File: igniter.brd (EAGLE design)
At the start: 29.2 x 63.5 mm, 9 parts, among them X1 Break, X2 IGN1, X3 IGN2

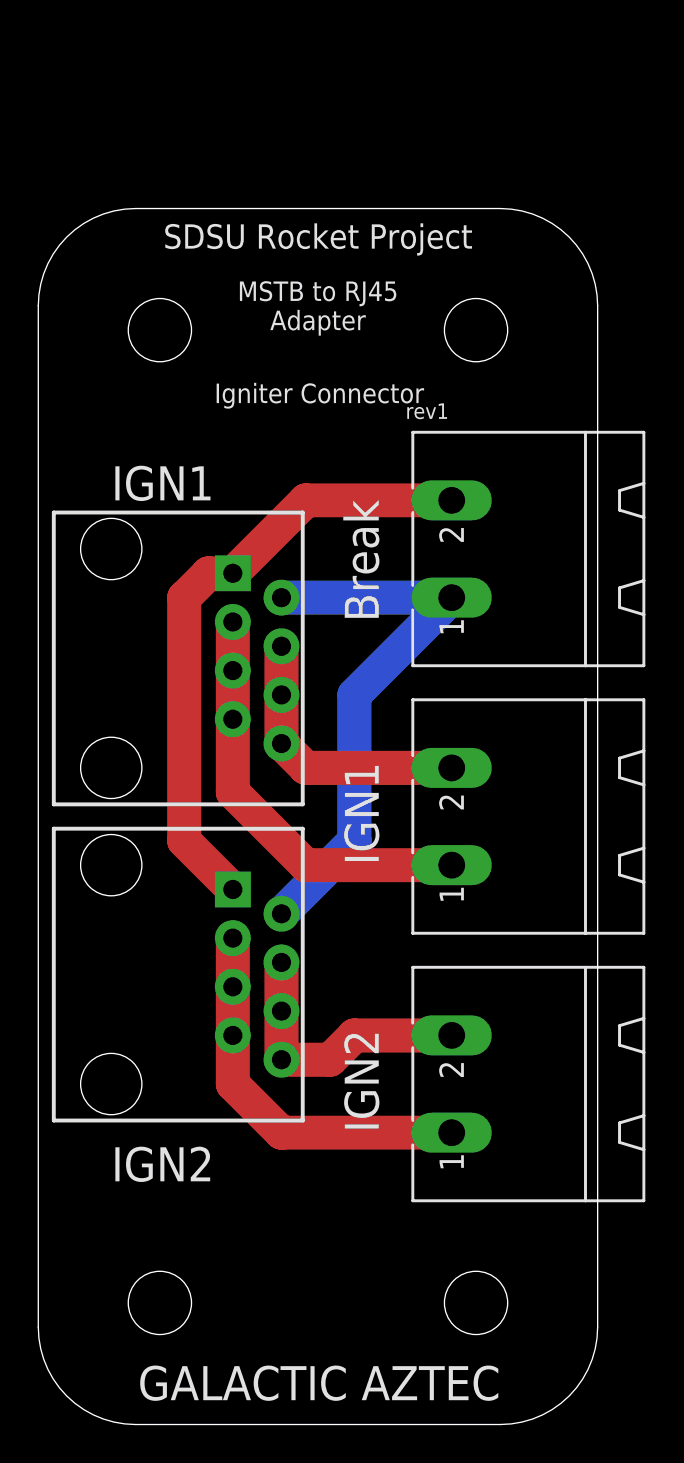
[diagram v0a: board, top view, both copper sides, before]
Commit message: Added ignition status LEDs. Separated break wire from ignition wires. Added SDSU logo.
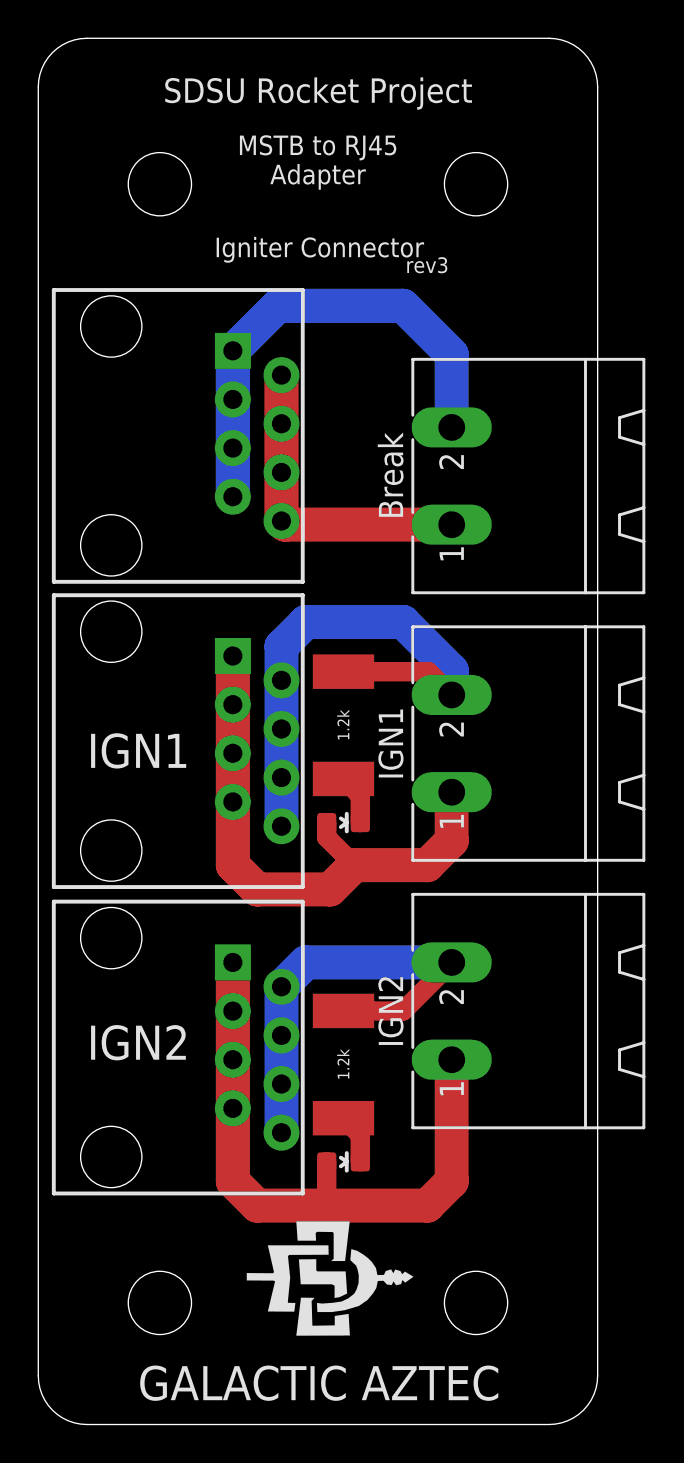
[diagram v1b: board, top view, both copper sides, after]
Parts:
- added BREAK: RJ45, SparkFun-Connectors:RJ45-8
- added D1, D2: RED, SparkFun-LED:LED-0603
- added FRAME1: (no value), SparkFun-Aesthetics:CREATIVE_COMMONS
- added R1, R2: 1.2k, SparkFun-Resistors:R2512
- moved U$3 7.62 mm to (22.9, 64.8)
- moved U$4 7.62 mm to (6.35, 64.8)
- moved IGNITER1 4.32 mm to (3.81, 35.7)
- moved IGNITER2 3.81 mm to (3.81, 19.7)
- moved X1 3.81 mm to (26.7, 49.5)
- moved X2 3.81 mm to (26.7, 35.6)
- moved X3 3.81 mm to (26.7, 21.6)
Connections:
- new net N$1: D1.C, R1.1
- new net N$2: D2.C, R2.1
- net 3V3: now also BREAK.1, BREAK.3, BREAK.5, BREAK.7; no longer IGNITER1.1, IGNITER2.1
- net BRK: now also BREAK.2, BREAK.4, BREAK.6, BREAK.8; no longer IGNITER1.2, IGNITER2.2
- net IGN1+: now also D1.A, IGNITER1.1
- net IGN1-: now also IGNITER1.2, R1.2
- net IGN2+: now also D2.A, IGNITER2.1
- net IGN2-: now also IGNITER2.2, R2.2
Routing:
- net IGN2+: track 20.1 -> 33.2 mm
- net IGN1-: track 14.5 -> 27.3 mm
- net BRK: track 29.1 -> 16.6 mm
- net IGN2-: track 14.5 -> 23.7 mm
- net 3V3: track 32.4 -> 24.9 mm
- net IGN1+: track 21.9 -> 29.3 mm
- net N$2: track 0.00 -> 2.64 mm
- net N$1: track 0.00 -> 2.64 mm
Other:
- board size 29.2 x 63.5 mm -> 29.2 x 72.4 mm
- board text added: "rev3"
- board text removed: "rev1"

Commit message: Updated to use more efficient LEDs. Decreased SMD resistor size to 0603.
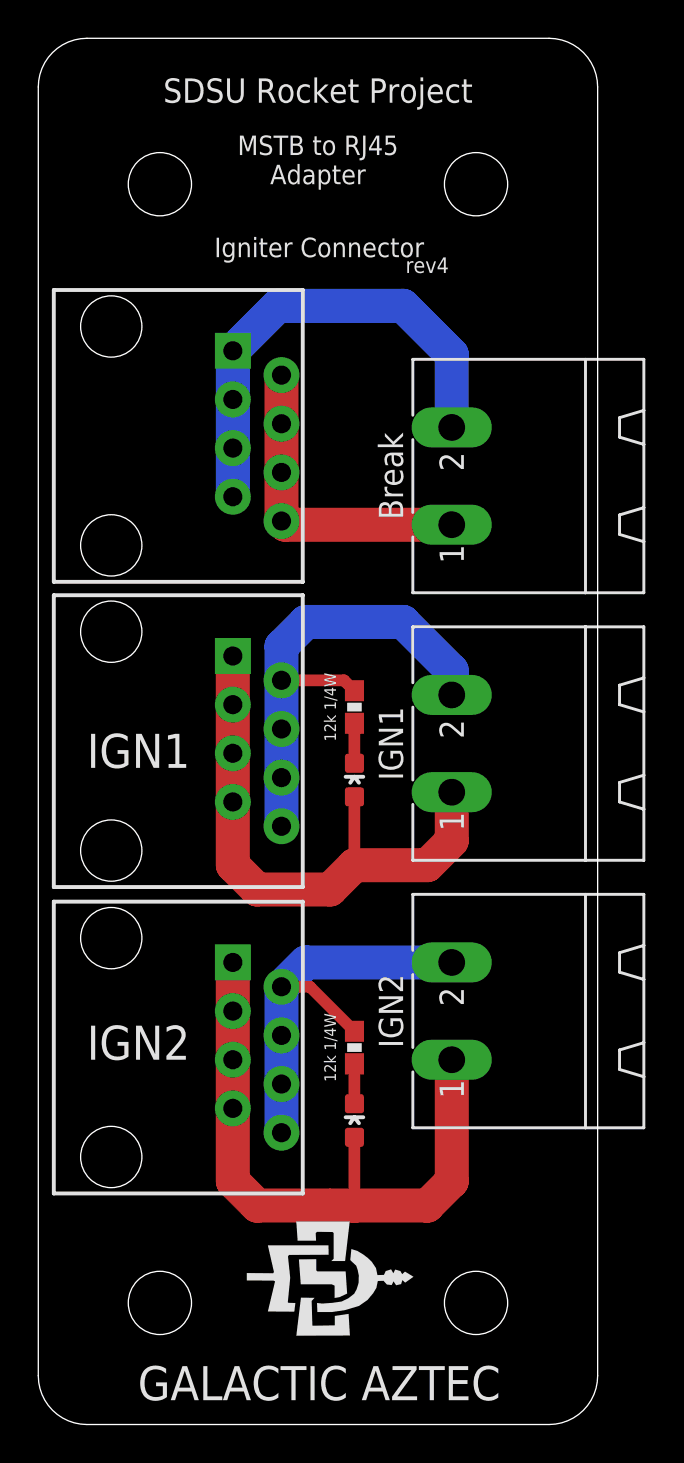
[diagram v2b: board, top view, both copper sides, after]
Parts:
- R1, R2: value 1.2k -> 12k 1/4W; device SparkFun-Resistors:R2512 -> SparkFun-Resistors:0603-RES
- moved D1 2.29 mm to (16.5, 33.7), turned to 0 degrees
- moved D2 2.23 mm to (16.5, 15.9), turned to 0 degrees
- moved R1 1.11 mm to (16.5, 37.5)
- moved R2 1.06 mm to (16.5, 19.7)
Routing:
- net IGN1-: track 27.3 -> 25.2 mm
- net IGN2-: track 23.7 -> 21.8 mm
- net IGN2+: track 33.2 -> 34.6 mm
- net IGN1+: track 29.3 -> 30.0 mm
- net N$2: track 2.64 -> 2.08 mm
- net N$1: track 2.64 -> 2.08 mm
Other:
- board text added: "rev4"
- board text removed: "rev3"
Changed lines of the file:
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@@
 <text x="14.605" y="70.2945" size="1.27" layer="25" font="vector" align="top-center">SDSU Rocket Project</text>
 <text x="14.6685" y="60.96" size="1.016" layer="25" font="vector" align="bottom-center">Igniter Connector</text>
-<text x="19.177" y="60.1345" size="0.8128" layer="25" font="vector">rev3</text>
+<text x="19.177" y="60.1345" size="0.8128" layer="25" font="vector">rev4</text>
 <text x="14.605" y="67.31" size="1.016" layer="25" font="vector" align="top-center">MSTB to RJ45
 Adapter</text>
@@
 <attribute name="PROD_ID" value="CONN-08506" x="25.4" y="68.1355" size="1.778" layer="27" rot="R270" display="off"/>
 </element>
-<element name="D1" library="SparkFun-LED" package="LED-0603" value="RED" x="15.9385" y="31.4325" smashed="yes" rot="R270"/>
+<element name="D1" library="SparkFun-LED" package="LED-0603" value="RED" x="16.51" y="33.655" smashed="yes"/>
 <element name="FRAME1" library="SparkFun-Aesthetics" package="CREATIVE_COMMONS" value="" x="46.99" y="0" rot="R90">
 <attribute name="VERSION" value="v01" x="46.99" y="0" size="1.778" layer="27" rot="R90" display="off"/>
 <attribute name="DESIGNER" value="NAME" x="46.99" y="0" size="1.778" layer="27" rot="R90" display="off"/>
 </element>
-<element name="R1" library="SparkFun-Resistors" package="R2512" value="1.2k" x="15.9385" y="36.5125" smashed="yes" rot="R90">
-<attribute name="VALUE" x="15.9385" y="36.5125" size="0.6096" layer="25" font="vector" rot="R90" align="center"/>
-</element>
-<element name="D2" library="SparkFun-LED" package="LED-0603" value="RED" x="15.9385" y="13.716" smashed="yes" rot="R270"/>
-<element name="R2" library="SparkFun-Resistors" package="R2512" value="1.2k" x="15.9385" y="18.796" smashed="yes" rot="R90">
-<attribute name="VALUE" x="15.9385" y="18.796" size="0.6096" layer="25" font="vector" rot="R90" align="center"/>
+<element name="R1" library="SparkFun-Resistors" package="0603-RES" value="12k 1/4W" x="16.51" y="37.465" smashed="yes" rot="R90">
+<attribute name="VALUE" x="15.24" y="37.465" size="0.6096" layer="25" font="vector" rot="R90" align="center"/>
+</element>
+<element name="D2" library="SparkFun-LED" package="LED-0603" value="RED" x="16.51" y="15.875" smashed="yes"/>
+<element name="R2" library="SparkFun-Resistors" package="0603-RES" value="12k 1/4W" x="16.51" y="19.685" smashed="yes" rot="R90">
+<attribute name="VALUE" x="15.24" y="19.685" size="0.6096" layer="25" font="vector" rot="R90" align="center"/>
 </element>
 </elements>
@@
 <wire x1="10.16" y1="37.592" x2="10.16" y2="40.132" width="1.778" layer="1"/>
 <contactref element="D1" pad="A"/>
-<wire x1="15.0615" y1="31.4325" x2="15.0615" y2="30.6585" width="1.016" layer="1"/>
-<wire x1="15.0615" y1="30.6585" x2="16.51" y2="29.21" width="1.016" layer="1"/>
+<wire x1="16.51" y1="32.778" x2="16.51" y2="29.21" width="0.6096" layer="1"/>
 </signal>
 <signal name="IGN1-">
@@
 <wire x1="12.7" y1="33.782" x2="12.7" y2="31.242" width="1.778" layer="16"/>
 <contactref element="R1" pad="2"/>
-<wire x1="15.9385" y1="39.3125" x2="20.3775" y2="39.3125" width="1.016" layer="1"/>
-<wire x1="20.3775" y1="39.3125" x2="21.59" y2="38.1" width="1.016" layer="1"/>
+<wire x1="12.7" y1="38.862" x2="15.963" y2="38.862" width="0.6096" layer="1"/>
+<wire x1="15.963" y1="38.862" x2="16.51" y2="38.315" width="0.6096" layer="1"/>
 </signal>
 <signal name="IGN2+">
@@
 <contactref element="D2" pad="A"/>
 <wire x1="21.59" y1="12.7" x2="20.32" y2="11.43" width="1.778" layer="1"/>
-<wire x1="20.32" y1="11.43" x2="15.24" y2="11.43" width="1.778" layer="1"/>
+<wire x1="20.32" y1="11.43" x2="16.51" y2="11.43" width="1.778" layer="1"/>
+<wire x1="16.51" y1="11.43" x2="15.24" y2="11.43" width="1.778" layer="1"/>
 <wire x1="15.24" y1="11.43" x2="11.43" y2="11.43" width="1.778" layer="1"/>
 <wire x1="15.633" y1="11.823" x2="15.24" y2="11.43" width="0.8128" layer="1"/>
-<wire x1="15.0615" y1="13.716" x2="15.0615" y2="11.6085" width="1.016" layer="1"/>
 <wire x1="15.0615" y1="11.6085" x2="15.24" y2="11.43" width="1.016" layer="1"/>
+<wire x1="16.51" y1="14.998" x2="16.51" y2="11.43" width="0.6096" layer="1"/>
 </signal>
 <signal name="IGN2-">
@@
 <wire x1="12.7" y1="22.86" x2="12.7" y2="20.32" width="1.778" layer="16"/>
 <contactref element="R2" pad="2"/>
-<wire x1="15.9385" y1="21.596" x2="19.056" y2="21.596" width="1.016" layer="1"/>
-<wire x1="19.056" y1="21.596" x2="21.59" y2="24.13" width="1.016" layer="1"/>
+<wire x1="16.51" y1="20.535" x2="14.185" y2="22.86" width="0.6096" layer="1"/>
+<wire x1="14.185" y1="22.86" x2="12.7" y2="22.86" width="0.6096" layer="1"/>
 </signal>
 <signal name="N$1">
 <contactref element="D1" pad="C"/>
 <contactref element="R1" pad="1"/>
-<wire x1="16.8155" y1="31.4325" x2="16.8155" y2="32.8355" width="1.016" layer="1"/>
-<wire x1="16.8155" y1="32.8355" x2="15.9385" y2="33.7125" width="1.016" layer="1"/>
+<wire x1="16.51" y1="36.615" x2="16.51" y2="34.532" width="0.6096" layer="1"/>
 </signal>
 <signal name="N$2">
 <contactref element="D2" pad="C"/>
 <contactref element="R2" pad="1"/>
-<wire x1="16.8155" y1="13.716" x2="16.8155" y2="15.119" width="1.016" layer="1"/>
-<wire x1="16.8155" y1="15.119" x2="15.9385" y2="15.996" width="1.016" layer="1"/>
+<wire x1="16.51" y1="18.835" x2="16.51" y2="16.752" width="0.6096" layer="1"/>
 </signal>
 </signals>
